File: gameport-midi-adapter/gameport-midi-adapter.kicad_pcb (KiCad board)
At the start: 2 copper layers, 84.6 x 51.6 mm, 11 parts, among them J1 DIN-5_180degree, J2 DIN-5_180degree, J3 Conn_01x15_Pin, J4 Conn_01x15_Socket, U1 4050

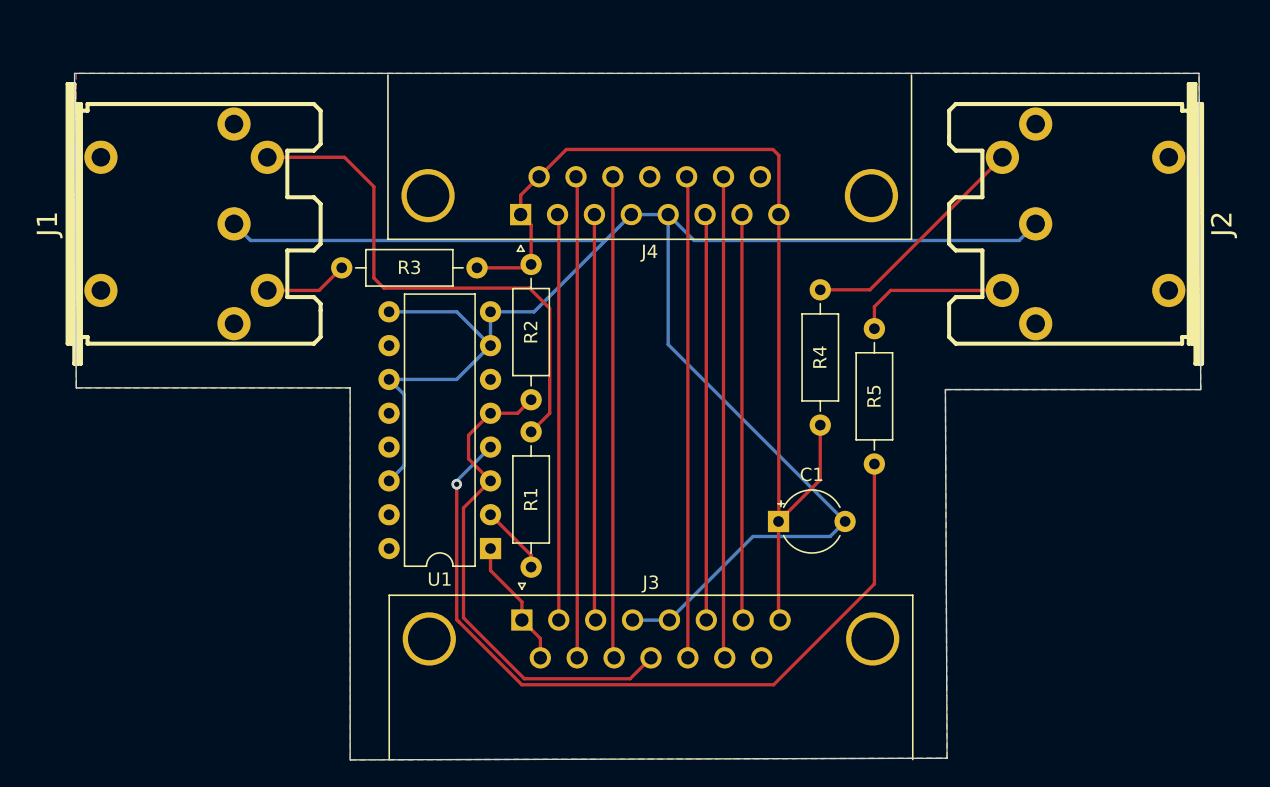
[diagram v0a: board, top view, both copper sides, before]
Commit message: Added Main README and updated gameport adapter
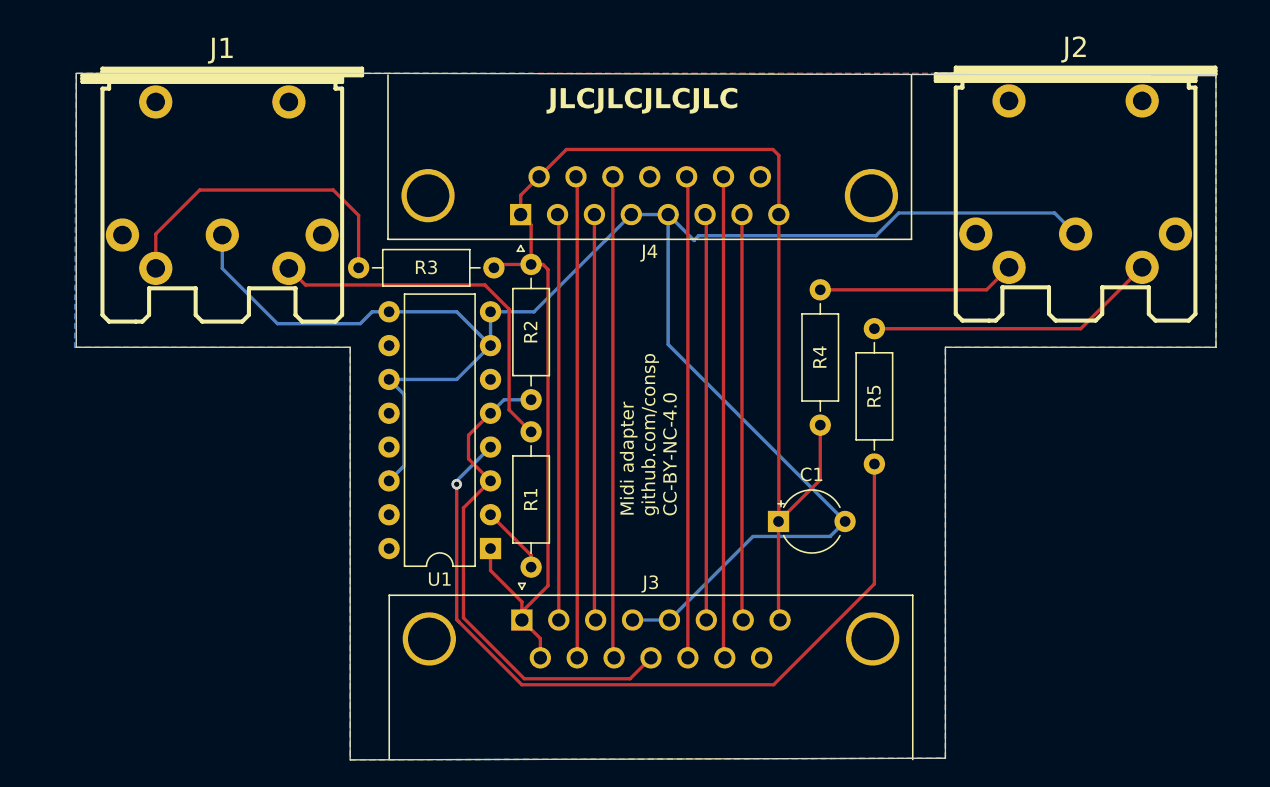
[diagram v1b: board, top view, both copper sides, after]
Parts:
- moved J1 3.02 mm to (123.5, 45.7), turned to 180 degrees
- moved J2 2.24 mm to (187.6, 45.6), turned to 180 degrees
- moved R3 1.27 mm to (133.7, 51.2)
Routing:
- net VCC: track 83.9 -> 111.6 mm
- net Net-(J1-Pad4): track 6.29 -> 23.9 mm
- net Net-(J1-Pad5): track 39.8 -> 27.7 mm
- net Net-(J2-Pad5): track 11.8 -> 22.0 mm
- net GND: track 149.8 -> 142.5 mm
- net Net-(J2-Pad4): track 17.8 -> 14.9 mm
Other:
- board size 84.6 x 51.6 mm -> 85.6 x 51.6 mm
- board text added: "JLCJLCJLCJLC"
- board text added: "Midi adapter github.com/consp CC-BY-NC-4.0"
